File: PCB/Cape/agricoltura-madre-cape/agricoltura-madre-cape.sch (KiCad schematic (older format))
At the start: 0 parts

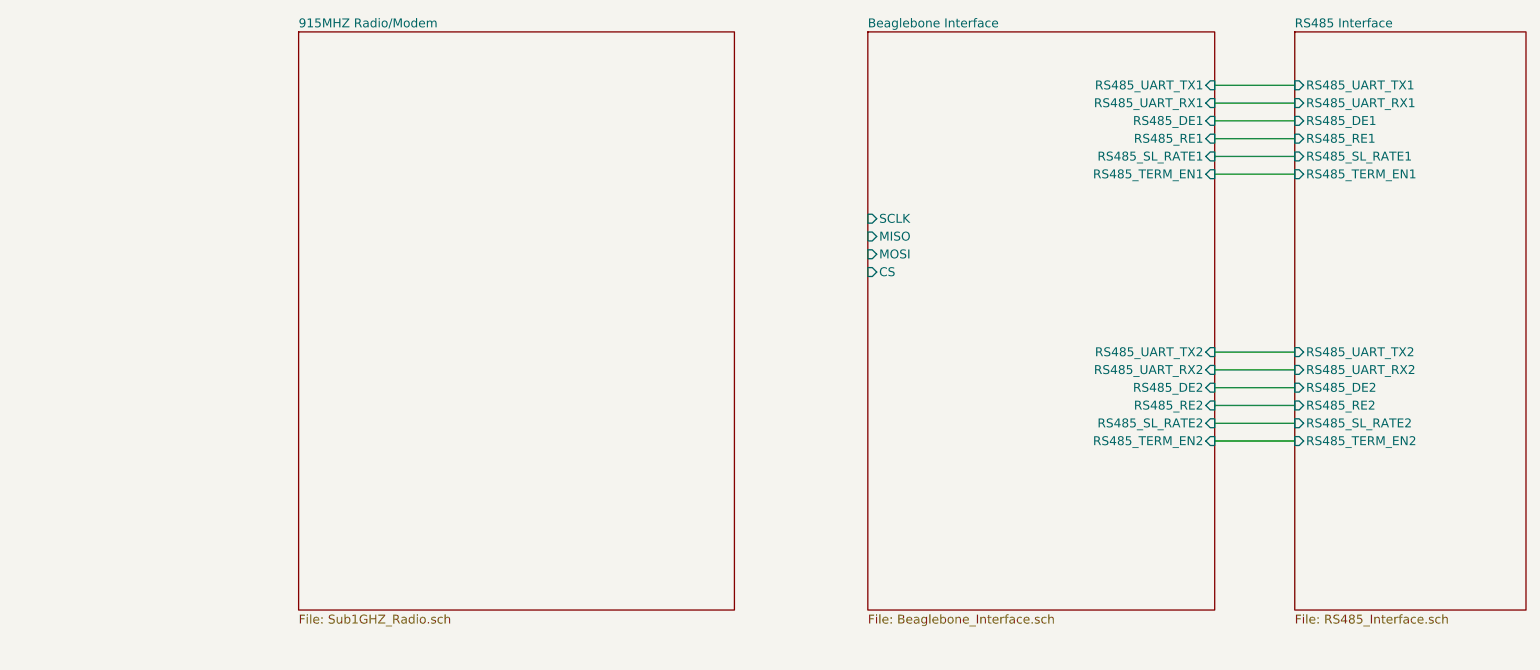
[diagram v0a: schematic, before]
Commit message: Datasheets and BBG version
Finished initial schematic for BBG Gateway version and added datasheets for ST sub 1GHZ RF hardware.
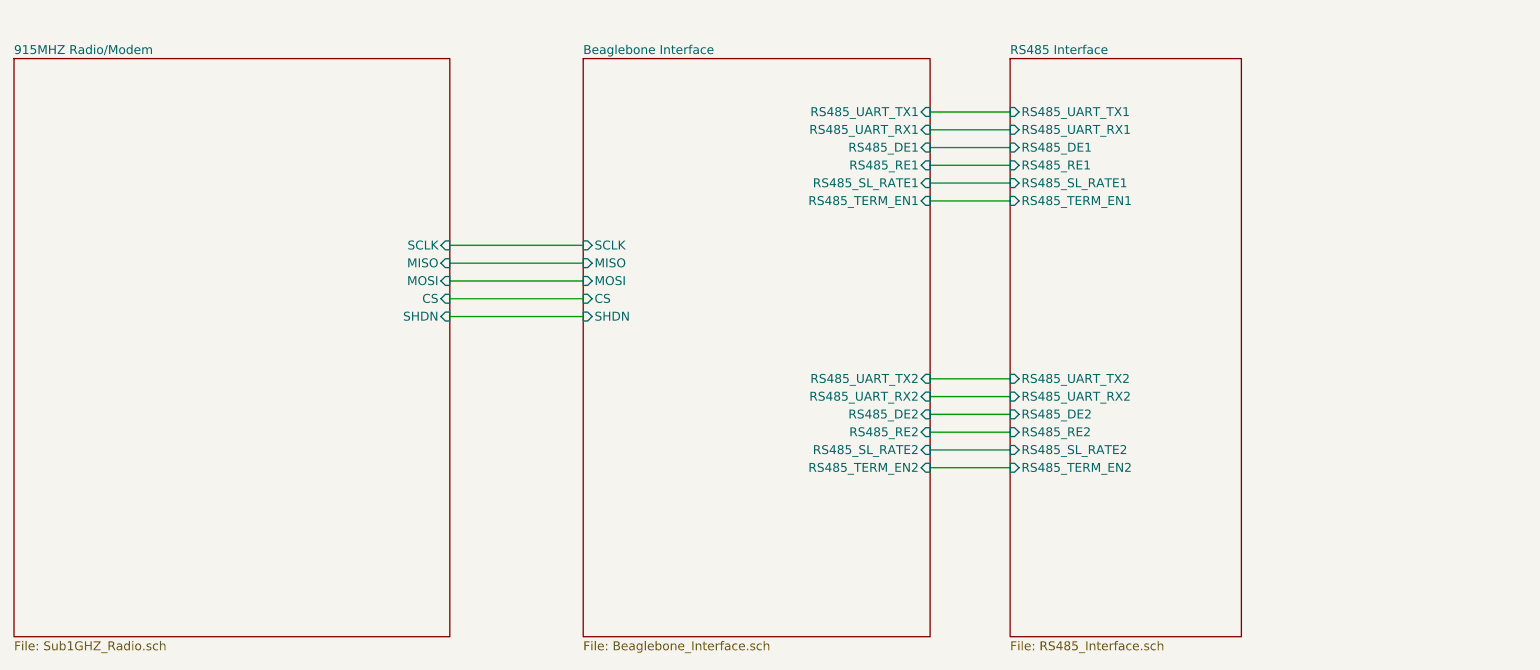
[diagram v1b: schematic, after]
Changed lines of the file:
@@
 $EndDescr
 $Sheet
-S 7300 1900 1950 3250
+S 5700 2050 1950 3250
 U 5EFF01A0
 F0 "Beaglebone Interface" 50
 F1 "Beaglebone_Interface.sch" 50
-F2 "RS485_UART_TX1" I R 9250 2200 50
-F3 "RS485_UART_RX1" I R 9250 2300 50
-F4 "RS485_UART_TX2" I R 9250 3700 50
-F5 "RS485_UART_RX2" I R 9250 3800 50
-F6 "RS485_DE2" I R 9250 3900 50
-F7 "RS485_DE1" I R 9250 2400 50
-F8 "RS485_SL_RATE2" I R 9250 4100 50
-F9 "RS485_SL_RATE1" I R 9250 2600 50
-F10 "RS485_TERM_EN1" I R 9250 2700 50
-F11 "RS485_RE1" I R 9250 2500 50
-F12 "RS485_RE2" I R 9250 4000 50
-F13 "RS485_TERM_EN2" I R 9250 4200 50
-F14 "SCLK" I L 7300 2950 50
-F15 "MISO" I L 7300 3050 50
-F16 "MOSI" I L 7300 3150 50
-F17 "CS" I L 7300 3250 50
+F2 "RS485_UART_TX1" I R 7650 2350 50
+F3 "RS485_UART_RX1" I R 7650 2450 50
+F4 "RS485_UART_TX2" I R 7650 3850 50
+F5 "RS485_UART_RX2" I R 7650 3950 50
+F6 "RS485_DE2" I R 7650 4050 50
+F7 "RS485_DE1" I R 7650 2550 50
+F8 "RS485_SL_RATE2" I R 7650 4250 50
+F9 "RS485_SL_RATE1" I R 7650 2750 50
+F10 "RS485_TERM_EN1" I R 7650 2850 50
+F11 "RS485_RE1" I R 7650 2650 50
+F12 "RS485_RE2" I R 7650 4150 50
+F13 "RS485_TERM_EN2" I R 7650 4350 50
+F14 "SCLK" I L 5700 3100 50
+F15 "MISO" I L 5700 3200 50
+F16 "MOSI" I L 5700 3300 50
+F17 "CS" I L 5700 3400 50
+F18 "SHDN" I L 5700 3500 50
 $EndSheet
 $Sheet
-S 9700 1900 1300 3250
+S 8100 2050 1300 3250
 U 5EFF8157
 F0 "RS485 Interface" 50
 F1 "RS485_Interface.sch" 50
-F2 "RS485_UART_TX1" I L 9700 2200 50
-F3 "RS485_UART_RX1" I L 9700 2300 50
-F4 "RS485_UART_TX2" I L 9700 3700 50
-F5 "RS485_UART_RX2" I L 9700 3800 50
-F6 "RS485_DE2" I L 9700 3900 50
-F7 "RS485_DE1" I L 9700 2400 50
-F8 "RS485_SL_RATE2" I L 9700 4100 50
-F9 "RS485_SL_RATE1" I L 9700 2600 50
-F10 "RS485_TERM_EN1" I L 9700 2700 50
-F11 "RS485_RE1" I L 9700 2500 50
-F12 "RS485_RE2" I L 9700 4000 50
-F13 "RS485_TERM_EN2" I L 9700 4200 50
+F2 "RS485_UART_TX1" I L 8100 2350 50
+F3 "RS485_UART_RX1" I L 8100 2450 50
+F4 "RS485_UART_TX2" I L 8100 3850 50
+F5 "RS485_UART_RX2" I L 8100 3950 50
+F6 "RS485_DE2" I L 8100 4050 50
+F7 "RS485_DE1" I L 8100 2550 50
+F8 "RS485_SL_RATE2" I L 8100 4250 50
+F9 "RS485_SL_RATE1" I L 8100 2750 50
+F10 "RS485_TERM_EN1" I L 8100 2850 50
+F11 "RS485_RE1" I L 8100 2650 50
+F12 "RS485_RE2" I L 8100 4150 50
+F13 "RS485_TERM_EN2" I L 8100 4350 50
 $EndSheet
 Wire Wire Line
-	9250 2200 9700 2200
+	7650 2350 8100 2350
 Wire Wire Line
-	9250 2300 9700 2300
+	7650 2450 8100 2450
 Wire Wire Line
-	9250 2400 9700 2400
+	7650 2550 8100 2550
 Wire Wire Line
-	9250 2500 9700 2500
+	7650 2650 8100 2650
 Wire Wire Line
-	9700 2600 9250 2600
+	8100 2750 7650 2750
 Wire Wire Line
-	9250 2700 9700 2700
+	7650 2850 8100 2850
 Wire Wire Line
-	9250 3700 9700 3700
+	7650 3850 8100 3850
 Wire Wire Line
-	9250 3800 9700 3800
+	7650 3950 8100 3950
 Wire Wire Line
-	9700 3900 9250 3900
+	8100 4050 7650 4050
 Wire Wire Line
-	9250 4000 9700 4000
+	7650 4150 8100 4150
 Wire Wire Line
-	9700 4100 9250 4100
+	8100 4250 7650 4250
 Wire Wire Line
-	9250 4200 9700 4200
+	7650 4350 8100 4350
 $Sheet
-S 4100 1900 2450 3250
+S 2500 2050 2450 3250
 U 5F03E6AE
 F0 "915MHZ Radio/Modem" 50
 F1 "Sub1GHZ_Radio.sch" 50
+F2 "SCLK" I R 4950 3100 50
+F3 "MISO" I R 4950 3200 50
+F4 "MOSI" I R 4950 3300 50
+F5 "CS" I R 4950 3400 50
+F6 "SHDN" I R 4950 3500 50
 $EndSheet
+Wire Wire Line
+	5700 3500 4950 3500
+Wire Wire Line
+	5700 3400 4950 3400
+Wire Wire Line
+	5700 3300 4950 3300
+Wire Wire Line
+	5700 3200 4950 3200
+Wire Wire Line
+	5700 3100 4950 3100
 $EndSCHEMATC
